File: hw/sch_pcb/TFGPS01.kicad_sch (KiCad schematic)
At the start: 75 parts, among them J1 SM10B-GHS-TB, J2 USBC_USB4105-GF-A, J3 SM06B-GHS-TB, J4 SM04B-GHS-TB, J5 SM08B-GHS-TB, M1 HOLE, M2 HOLE, M3 HOLE, M4 HOLE, Q1 BC817-25, Q2 BC817-25, Q3 BC817-25, U1 MIC5504-3.3YM5, U2 USBLC6-2SC6, U3 NEO-M8P, U4 MAX2655

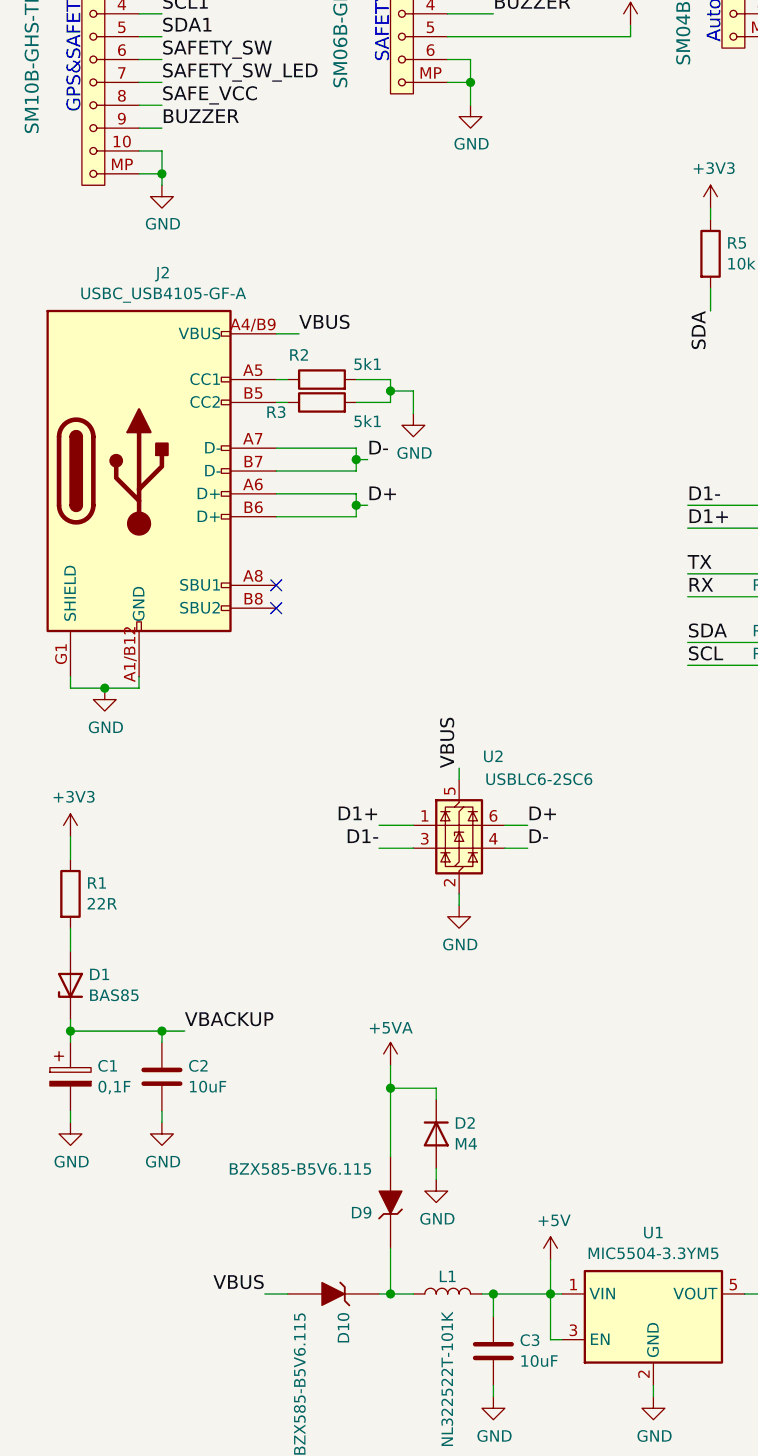
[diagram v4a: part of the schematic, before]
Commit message: Update footprints resolve DRC and ERC issues.
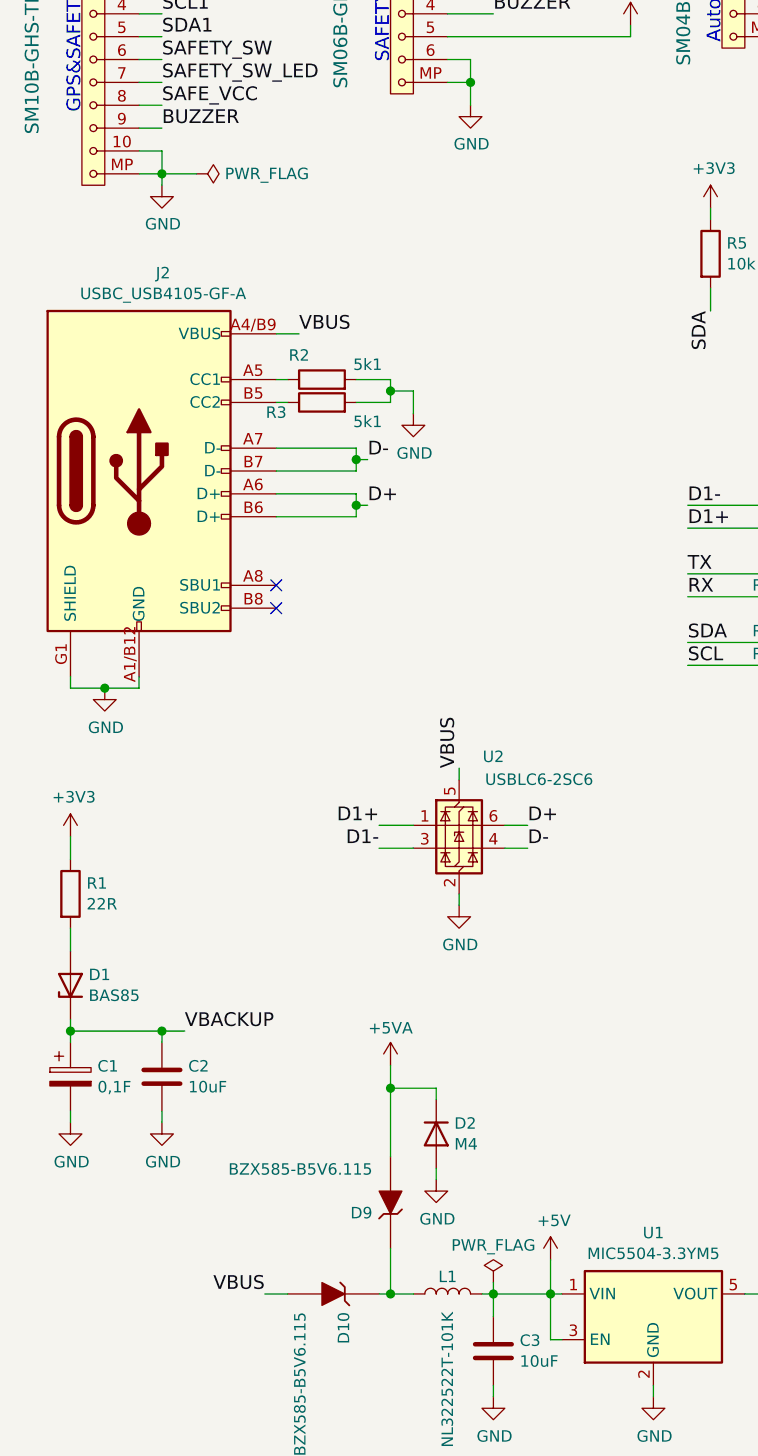
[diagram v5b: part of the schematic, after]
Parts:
- C10, C11, C12, C13, C14, C15, C2, C3, C4, C5, C6, C7, C8, C9: footprint Mlab_R:SMD-0805 -> Capacitor_SMD:C_0805_2012Metric
- L2: footprint Mlab_R:SMD-0805 -> Inductor_SMD:L_0805_2012Metric
- R1, R10, R11, R12, R13, R14, R15, R16, R17, R18, R19, R2, R20, R21, R22, R23, R24, R25, R26, R27, R28, R3, R4, R5, R6, R7, R8, R9: footprint Mlab_R:SMD-0805 -> Resistor_SMD:R_0805_2012Metric
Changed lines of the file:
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@@
 	(wire
 		(pts
+			(xy 29.21 46.99) (xy 33.02 46.99)
+		)
+		(stroke
+			(width 0)
+			(type default)
+		)
+	)
+	(wire
+		(pts
 			(xy 87.63 83.82) (xy 99.06 83.82)
 		)
@@
 	(wire
 		(pts
+			(xy 66.04 170.18) (xy 66.04 171.45)
+		)
+		(stroke
+			(width 0)
+			(type default)
+		)
+	)
+	(wire
+		(pts
 			(xy 54.61 166.37) (xy 54.61 171.45)
 		)
@@
 			)
 		)
-		(property "Footprint" "Mlab_R:SMD-0805"
+		(property "Footprint" "Resistor_SMD:R_0805_2012Metric"
 			(at 17.272 127 90)
 			(effects
@@
 			)
 		)
-		(property "Footprint" "Mlab_R:SMD-0805"
+		(property "Footprint" "Capacitor_SMD:C_0805_2012Metric"
 			(at 67.0052 181.61 0)
 			(effects
@@
 			)
 		)
-		(property "Footprint" "Mlab_R:SMD-0805"
+		(property "Footprint" "Capacitor_SMD:C_0805_2012Metric"
 			(at 98.7552 181.61 0)
 			(effects
@@
 			)
 		)
-		(property "Footprint" "Mlab_R:SMD-0805"
+		(property "Footprint" "Resistor_SMD:R_0805_2012Metric"
 			(at 116.332 185.42 90)
 			(effects
@@
 			)
 		)
-		(property "Footprint" "Mlab_R:SMD-0805"
+		(property "Footprint" "Resistor_SMD:R_0805_2012Metric"
 			(at 149.352 127 90)
 			(effects
@@
 			)
 		)
-		(property "Footprint" "Mlab_R:SMD-0805"
+		(property "Footprint" "Resistor_SMD:R_0805_2012Metric"
 			(at 158.242 127 90)
 			(effects
@@
 			)
 		)
-		(property "Footprint" "Mlab_R:SMD-0805"
+		(property "Footprint" "Resistor_SMD:R_0805_2012Metric"
 			(at 155.702 168.91 90)
 			(effects
@@
 			)
 		)
-		(property "Footprint" "Mlab_R:SMD-0805"
+		(property "Footprint" "Resistor_SMD:R_0805_2012Metric"
 			(at 102.87 82.042 90)
 			(effects
@@
 			)
 		)
-		(property "Footprint" "Mlab_R:SMD-0805"
+		(property "Footprint" "Resistor_SMD:R_0805_2012Metric"
 			(at 102.87 84.582 90)
 			(effects
@@
 			)
 		)
-		(property "Footprint" "Mlab_R:SMD-0805"
+		(property "Footprint" "Resistor_SMD:R_0805_2012Metric"
 			(at 102.87 89.662 90)
 			(effects
@@
 			)
 		)
-		(property "Footprint" "Mlab_R:SMD-0805"
+		(property "Footprint" "Resistor_SMD:R_0805_2012Metric"
 			(at 102.87 92.202 90)
 			(effects
@@
 			)
 		)
-		(property "Footprint" "Mlab_R:SMD-0805"
+		(property "Footprint" "Resistor_SMD:R_0805_2012Metric"
 			(at 102.87 97.282 90)
 			(effects
@@
 			)
 		)
-		(property "Footprint" "Mlab_R:SMD-0805"
+		(property "Footprint" "Resistor_SMD:R_0805_2012Metric"
 			(at 102.87 99.822 90)
 			(effects
@@
 			)
 		)
-		(property "Footprint" "Mlab_R:SMD-0805"
+		(property "Footprint" "Capacitor_SMD:C_0805_2012Metric"
 			(at 113.9952 71.12 0)
 			(effects
@@
 			)
 		)
-		(property "Footprint" "Mlab_R:SMD-0805"
+		(property "Footprint" "Capacitor_SMD:C_0805_2012Metric"
 			(at 108.9152 181.61 0)
 			(effects
@@
 			)
 		)
-		(property "Footprint" "Mlab_R:SMD-0805"
+		(property "Footprint" "Resistor_SMD:R_0805_2012Metric"
 			(at 88.392 55.88 90)
 			(effects
@@
 			)
 		)
-		(property "Footprint" "Mlab_R:SMD-0805"
+		(property "Footprint" "Resistor_SMD:R_0805_2012Metric"
 			(at 97.282 55.88 90)
 			(effects
@@
 			)
 		)
-		(property "Footprint" "Mlab_R:SMD-0805"
+		(property "Footprint" "Resistor_SMD:R_0805_2012Metric"
 			(at 129.54 31.242 90)
 			(effects
@@
 			)
 		)
-		(property "Footprint" "Mlab_R:SMD-0805"
+		(property "Footprint" "Capacitor_SMD:C_0805_2012Metric"
 			(at 180.6448 83.82 0)
 			(effects
@@
 			)
 		)
-		(property "Footprint" "Mlab_R:SMD-0805"
+		(property "Footprint" "Capacitor_SMD:C_0805_2012Metric"
 			(at 206.7052 91.44 0)
 			(effects
@@
 			)
 		)
-		(property "Footprint" "Mlab_R:SMD-0805"
+		(property "Footprint" "Resistor_SMD:R_0805_2012Metric"
 			(at 154.178 38.1 90)
 			(effects
@@
 			)
 		)
-		(property "Footprint" "Mlab_R:SMD-0805"
+		(property "Footprint" "Capacitor_SMD:C_0805_2012Metric"
 			(at 134.3152 67.31 0)
 			(effects
@@
 			)
 		)
-		(property "Footprint" "Mlab_R:SMD-0805"
+		(property "Footprint" "Capacitor_SMD:C_0805_2012Metric"
 			(at 246.0752 119.38 0)
 			(effects
@@
 			)
 		)
-		(property "Footprint" "Mlab_R:SMD-0805"
+		(property "Footprint" "Resistor_SMD:R_0805_2012Metric"
 			(at 46.99 71.628 90)
 			(effects
@@
 			)
 		)
-		(property "Footprint" "Mlab_R:SMD-0805"
+		(property "Footprint" "Resistor_SMD:R_0805_2012Metric"
 			(at 223.52 42.418 90)
 			(effects
@@
 			)
 		)
-		(property "Footprint" "Mlab_R:SMD-0805"
+		(property "Footprint" "Resistor_SMD:R_0805_2012Metric"
 			(at 233.172 115.57 90)
 			(effects
@@
 			)
 		)
-		(property "Footprint" "Mlab_R:SMD-0805"
+		(property "Footprint" "Resistor_SMD:R_0805_2012Metric"
 			(at 129.54 28.702 90)
 			(effects
@@
 			)
 		)
-		(property "Footprint" "Mlab_R:SMD-0805"
+		(property "Footprint" "Inductor_SMD:L_0805_2012Metric"
 			(at 250.19 99.06 0)
 			(effects
@@
 	)
 	(symbol
+		(lib_id "power:PWR_FLAG")
+		(at 33.02 46.99 270)
+		(unit 1)
+		(exclude_from_sim no)
+		(in_bom yes)
+		(on_board yes)
+		(dnp no)
+		(fields_autoplaced yes)
+		(property "Reference" "#FLG02"
+			(at 34.925 46.99 0)
+			(effects
+				(font
+					(size 1.27 1.27)
+				)
+				(hide yes)
+			)
+		)
+		(property "Value" "PWR_FLAG"
+			(at 36.195 46.99 90)
+			(effects
+				(font
+					(size 1.27 1.27)
+				)
+				(justify left)
+			)
+		)
+		(property "Footprint" ""
+			(at 33.02 46.99 0)
+			(effects
+				(font
+					(size 1.27 1.27)
+				)
+				(hide yes)
+			)
+		)
+		(property "Datasheet" "~"
+			(at 33.02 46.99 0)
+			(effects
+				(font
+					(size 1.27 1.27)
+				)
+				(hide yes)
+			)
+		)
+		(property "Description" "Special symbol for telling ERC where power comes from"
+			(at 33.02 46.99 0)
+			(effects
+				(font
+					(size 1.27 1.27)
+				)
+				(hide yes)
+			)
+		)
+		(pin "1"
+		)
+		(instances
+			(project "TFGPS01"
+				(path "/73a4ed73-0a5d-4a8d-ac5b-dfe222bafbe2"
+					(reference "#FLG02")
+					(unit 1)
+				)
+			)
+		)
+	)
+	(symbol
 		(lib_id "Device:C")
 		(at 212.09 99.06 90)
@@
 			)
 		)
-		(property "Footprint" "Mlab_R:SMD-0805"
+		(property "Footprint" "Capacitor_SMD:C_0805_2012Metric"
 			(at 215.9 98.0948 0)
 			(effects
@@
 			)
 		)
-		(property "Footprint" "Mlab_R:SMD-0805"
+		(property "Footprint" "Resistor_SMD:R_0805_2012Metric"
 			(at 129.54 16.002 90)
 			(effects
@@
 			)
 		)
-		(property "Footprint" "Mlab_R:SMD-0805"
+		(property "Footprint" "Capacitor_SMD:C_0805_2012Metric"
 			(at 255.5748 101.6 0)
 			(effects
@@
 			)
 		)
-		(property "Footprint" "Mlab_R:SMD-0805"
+		(property "Footprint" "Capacitor_SMD:C_0805_2012Metric"
 			(at 193.3448 83.82 0)
 			(effects
@@
 	)
 	(symbol
+		(lib_id "power:PWR_FLAG")
+		(at 66.04 170.18 0)
+		(unit 1)
+		(exclude_from_sim no)
+		(in_bom yes)
+		(on_board yes)
+		(dnp no)
+		(fields_autoplaced yes)
+		(property "Reference" "#FLG03"
+			(at 66.04 168.275 0)
+			(effects
+				(font
+					(size 1.27 1.27)
+				)
+				(hide yes)
+			)
+		)
+		(property "Value" "PWR_FLAG"
+			(at 66.04 166.0469 0)
+			(effects
+				(font
+					(size 1.27 1.27)
+				)
+			)
+		)
+		(property "Footprint" ""
+			(at 66.04 170.18 0)
+			(effects
+				(font
+					(size 1.27 1.27)
+				)
+				(hide yes)
+			)
+		)
+		(property "Datasheet" "~"
+			(at 66.04 170.18 0)
+			(effects
+				(font
+					(size 1.27 1.27)
+				)
+				(hide yes)
+			)
+		)
+		(property "Description" "Special symbol for telling ERC where power comes from"
+			(at 66.04 170.18 0)
+			(effects
+				(font
+					(size 1.27 1.27)
+				)
+				(hide yes)
+			)
+		)
+		(pin "1"
+		)
+		(instances
+			(project "TFGPS01"
+				(path "/73a4ed73-0a5d-4a8d-ac5b-dfe222bafbe2"
+					(reference "#FLG03")
+					(unit 1)
+				)
+			)
+		)
+	)
+	(symbol
 		(lib_id "Device:C")
 		(at 262.89 99.06 90)
@@
 			)
 		)
-		(property "Footprint" "Mlab_R:SMD-0805"
+		(property "Footprint" "Capacitor_SMD:C_0805_2012Metric"
 			(at 266.7 98.0948 0)
 			(effects
@@
 			)
 		)
-		(property "Footprint" "Mlab_R:SMD-0805"
+		(property "Footprint" "Resistor_SMD:R_0805_2012Metric"
 			(at 46.99 74.168 90)
 			(effects
@@
 			)
 		)
-		(property "Footprint" "Mlab_R:SMD-0805"
+		(property "Footprint" "Resistor_SMD:R_0805_2012Metric"
 			(at 144.78 182.118 90)
 			(effects
@@
 			)
 		)
-		(property "Footprint" "Mlab_R:SMD-0805"
+		(property "Footprint" "Resistor_SMD:R_0805_2012Metric"
 			(at 215.392 87.63 90)
 			(effects
@@
 			)
 		)
-		(property "Footprint" "Mlab_R:SMD-0805"
+		(property "Footprint" "Resistor_SMD:R_0805_2012Metric"
 			(at 157.48 47.498 90)
 			(effects
@@
 			)
 		)
-		(property "Footprint" "Mlab_R:SMD-0805"
+		(property "Footprint" "Capacitor_SMD:C_0805_2012Metric"
 			(at 213.36 39.6748 0)
 			(effects
@@
 			)
 		)
-		(property "Footprint" "Mlab_R:SMD-0805"
+		(property "Footprint" "Capacitor_SMD:C_0805_2012Metric"
 			(at 30.1752 151.13 0)
 			(effects
@@
 			)
 		)
-		(property "Footprint" "Mlab_R:SMD-0805"
+		(property "Footprint" "Resistor_SMD:R_0805_2012Metric"
 			(at 129.54 18.542 90)
 			(effects
@@
 			)
 		)
-		(property "Footprint" "Mlab_R:SMD-0805"
+		(property "Footprint" "Resistor_SMD:R_0805_2012Metric"
 			(at 129.54 21.082 90)
 			(effects
@@
 			)
 		)
-		(property "Footprint" "Mlab_R:SMD-0805"
+		(property "Footprint" "Resistor_SMD:R_0805_2012Metric"
 			(at 186.69 76.708 90)
 			(effects
@@
 			)
 		)
-		(property "Footprint" "Mlab_R:SMD-0805"
+		(property "Footprint" "Resistor_SMD:R_0805_2012Metric"
 			(at 168.402 34.29 90)
 			(effects
